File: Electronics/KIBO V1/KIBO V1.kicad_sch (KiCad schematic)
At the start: 46 parts, among them M1 Motor_Servo, M10 Motor_Servo, M11 Motor_Servo, M12 Motor_Servo, M13 Motor_DC, M14 Motor_DC, M15 Motor_DC, M16 Motor_DC, M17 Fan, M18 uMotor_Servo, M19 uMotor_Servo, M2 Motor_Servo, M20 uMotor_Servo, M21 uMotor_Servo, M3 Motor_Servo, M4 Motor_Servo, M5 Motor_Servo, M6 Motor_Servo, M7 Motor_Servo, M8 Motor_Servo, M9 Motor_Servo, Q1 TIP120, SW1 SW_SPST, U1 HC-SR04, U3 ESP32-DEVKITC, U4 GY-521, U5 DM-OLED096-636, U6 OV7670

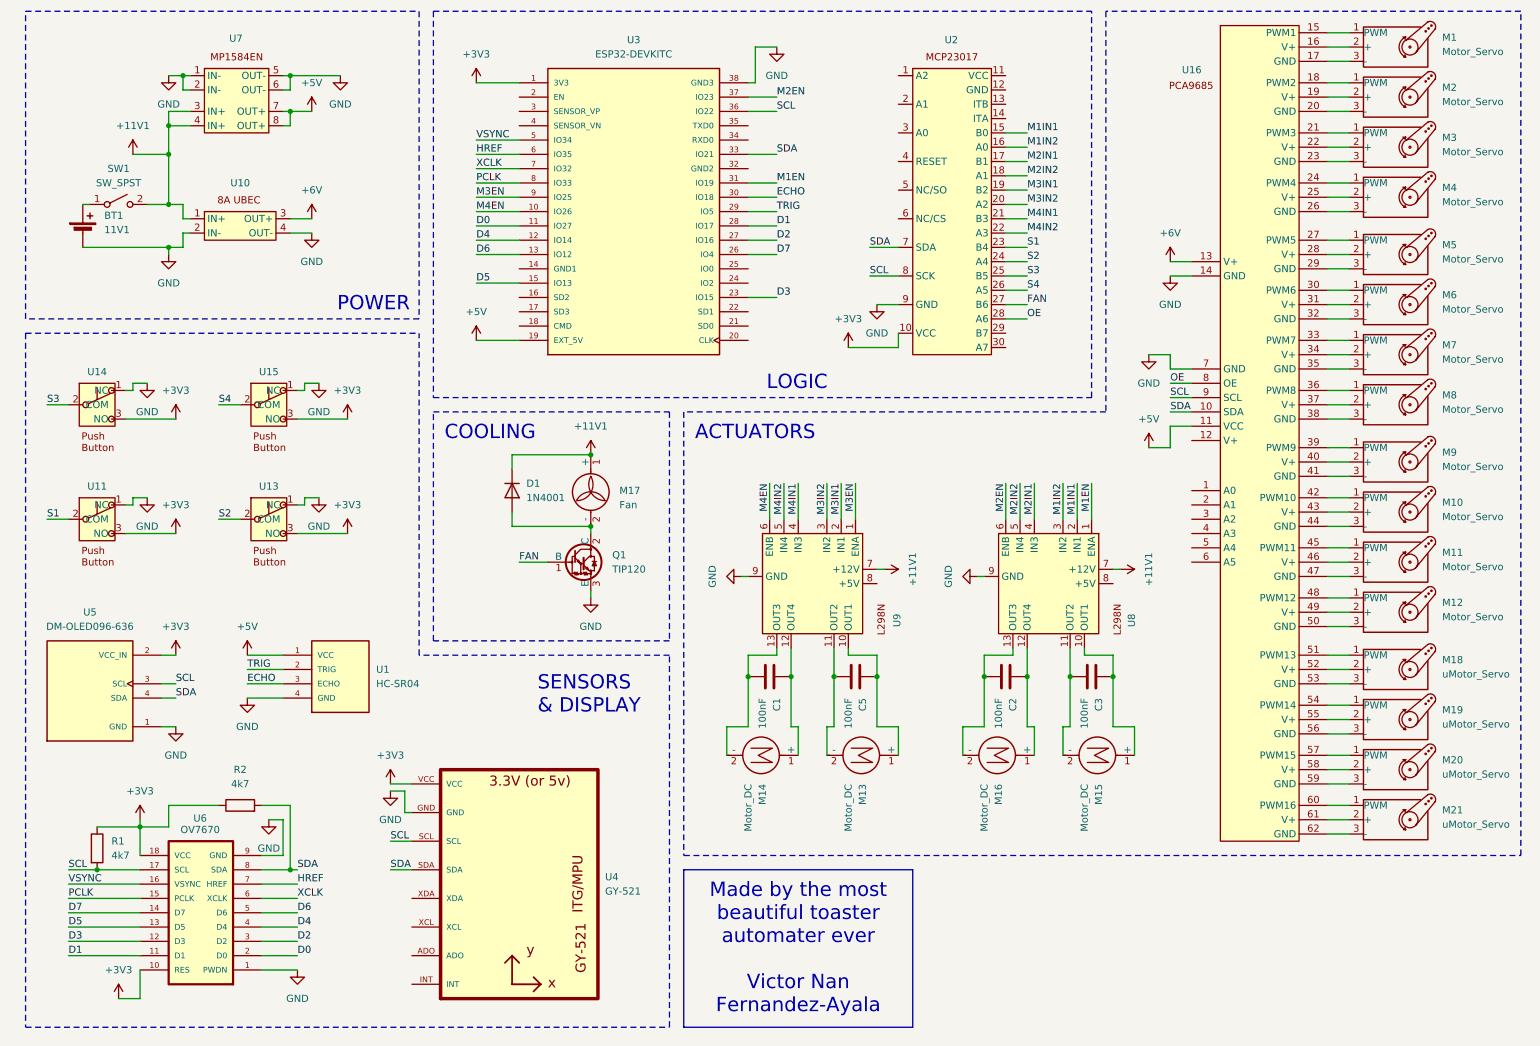
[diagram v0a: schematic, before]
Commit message: feat: added RGB LEDs and ESP32-CAM with PIR to schematic
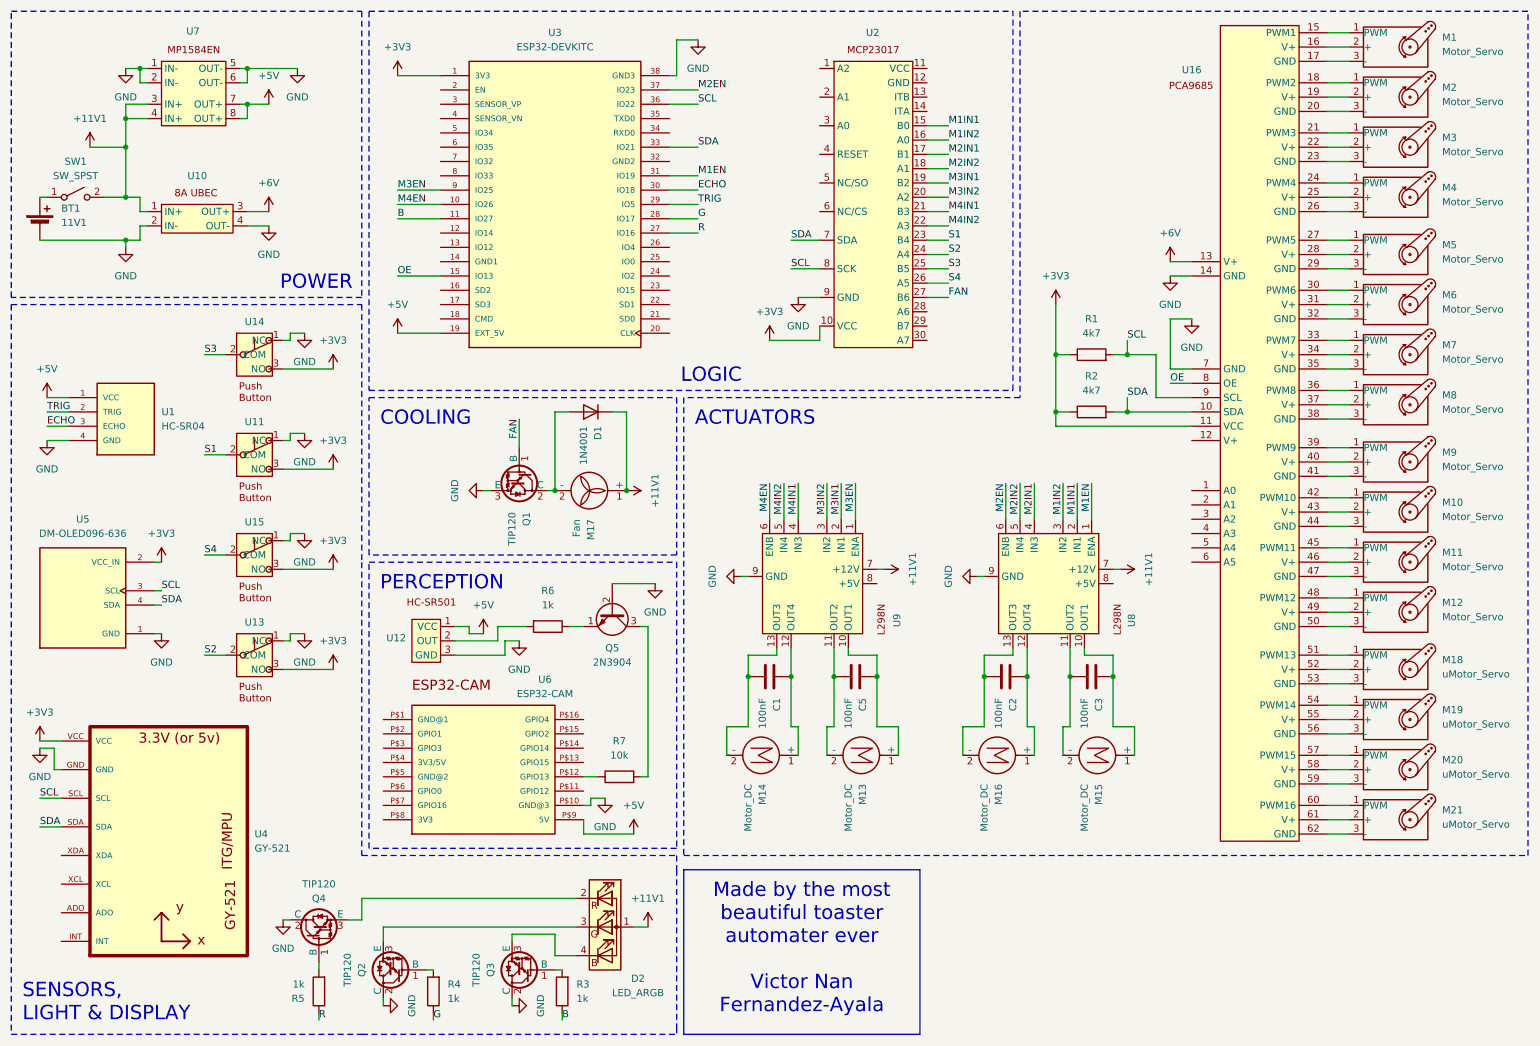
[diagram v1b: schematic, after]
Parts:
- removed U6: OV7670, OV7670:OV7670, symbol OV7670:OV7670_RST_PWDN
- added D2: LED_ARGB, symbol Device:LED_ARGB
- added Q2, Q3, Q4: TIP120, Package_TO_SOT_THT:TO-220-3_Vertical, symbol Transistor_BJT:TIP120
- added Q5: 2N3904, Package_TO_SOT_THT:TO-92_Inline, symbol Transistor_BJT:2N3904
- added R3, R4, R5, R6: 1k, symbol Device:R
- added R7: 10k, symbol Device:R
- added U12: ~, symbol PIRSensor_AZDelivery_HCSR501:HC-SR501
- added U6: ESP32-CAM, ESP32-CAM:ESP32-CAM, symbol ESP32-CAM:ESP32-CAM
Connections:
- net D5 is gone; now on net OE: U3.15 (IO13)
- net +11V1: now also D2.1 (A)
- net +3V3: now also U16.11 (VCC)
- net +5V: now also U12.1 (VCC), U6.P$9 (5V); no longer U16.11 (VCC)
- net GND: now also Q2.2 (C), Q3.2 (C), Q4.2 (C), Q5.2 (B), U12.3 (GND), U6.P$10 (GND@3)
- net OE: no longer U2.28 (A6)
- net D0 renamed B
- net B: now also R3.1
- net D1 renamed G
- net G: now also R4.1
- net D2 renamed R
- net R: now also R5.1
- net D3: no longer names the net of U3.23 (IO15)
- net D4: no longer names the net of U3.12 (IO14)
- net D6: no longer names the net of U3.13 (IO12)
- net D7: no longer names the net of U3.26 (IO4)
- net HREF: no longer names the net of U3.6 (IO35)
- net PCLK: no longer names the net of U3.8 (IO33)
- net VSYNC: no longer names the net of U3.5 (IO34)
- net XCLK: no longer names the net of U3.7 (IO32)
- new net: Q3.1 (B), R3.2
- new net: D2.4 (BK), Q3.3 (E)
- new net: D2.2 (RK), Q4.3 (E)
- new net: D2.3 (GK), Q2.3 (E)
- new net: Q2.1 (B), R4.2
- new net: R6.2, U12.2 (OUT)
- new net: Q4.1 (B), R5.2
- new net: R7.1, U6.P$12 (GPIO13)
- new net: Q5.3 (C), R7.2
- new net: Q5.1 (E), R6.1
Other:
- moved on the sheet: BT1, D1, M17, Q1, SW1, U1, U10, U11, U13, U14, U15, U2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

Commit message: feat: corrected schematics, finished all footprints and checked ERC
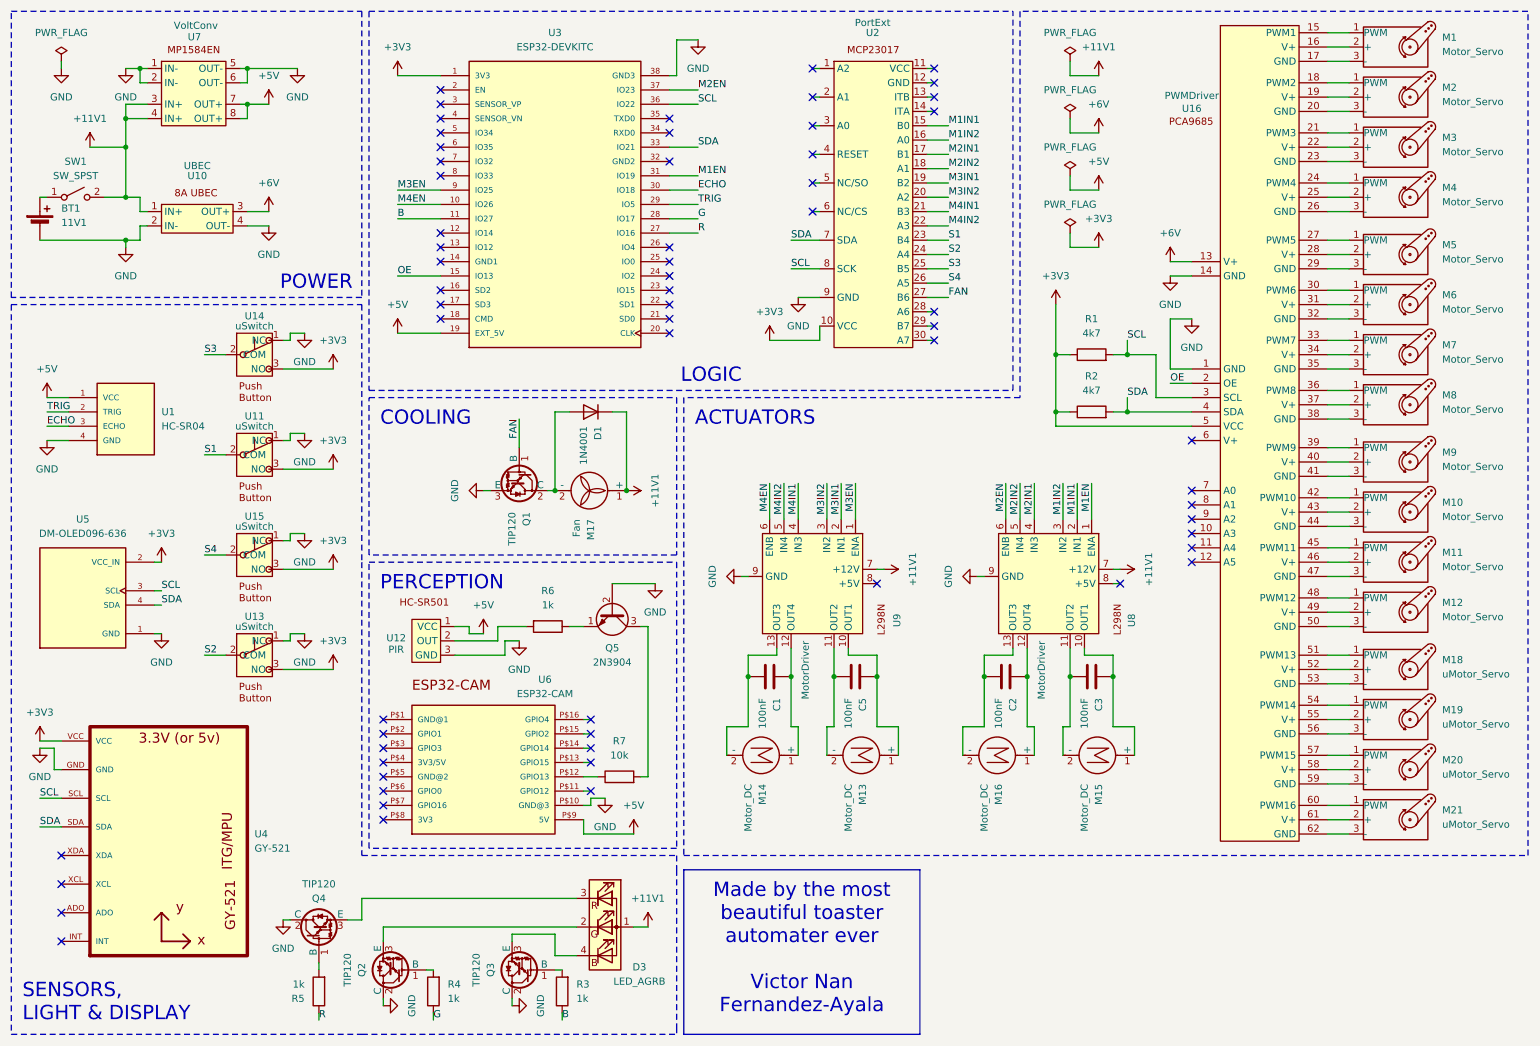
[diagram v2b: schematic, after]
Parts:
- removed D2: LED_ARGB, symbol Device:LED_ARGB
- added D3: LED_AGRB, Connector_PinHeader_2.54mm:PinHeader_1x04_P2.54mm_Vertical, symbol Device:LED_AGRB
- BT1: footprint (none) -> 2xBattery_Wire_Pads:2xBatterty_Wire_Pads
- C1, C2, C3, C5: footprint (none) -> Capacitor_THT:C_Disc_D5.0mm_W2.5mm_P5.00mm
- M17, SW1: footprint (none) -> Connector_Wire:SolderWire-0.75sqmm_1x02_P4.8mm_D1.25mm_OD2.3mm
- R1, R2, R3, R4, R5, R6, R7: footprint (none) -> Resistor_THT:R_Axial_DIN0207_L6.3mm_D2.5mm_P7.62mm_Horizontal
- U1: footprint HC-SR04:XCVR_HC-SR04 -> Connector_PinHeader_2.54mm:PinHeader_1x04_P2.54mm_Vertical
- U10: value ~ -> UBEC; footprint (none) -> 2xBattery_Wire_Pads:2xBatterty_Wire_Pads
- U11, U13, U14, U15: value ~ -> uSwitch; footprint (none) -> Connector_PinHeader_2.54mm:PinHeader_1x03_P2.54mm_Vertical
- U12: value ~ -> PIR
- U16: value ~ -> PWMDriver; footprint (none) -> Connector_PinHeader_2.54mm:PinHeader_1x05_P2.54mm_Vertical
- U2: value ~ -> PortExt; footprint (none) -> MCP23017:MCP23017
- U5: footprint DM-OLED096-636:MODULE_DM-OLED096-636 -> Connector_PinHeader_2.54mm:PinHeader_1x04_P2.54mm_Vertical
- U7: value ~ -> VoltConv; footprint (none) -> MP-1584EN:MP-1584EN
- U8, U9: value ~ -> MotorDriver; footprint (none) -> Connector_PinHeader_2.54mm:PinHeader_1x06_P2.54mm_Vertical
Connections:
- net +11V1: now also D3.1 (A)
- net +3V3: now also U16.5 (VCC); no longer U16.11 (VCC)
- net GND: now also U16.1 (GND); no longer U16.7 (GND)
- net OE: now also U16.2 (OE); no longer U16.8 (OE)
- net SCL: now also U16.3 (SCL); no longer U16.9 (SCL)
- net SDA: now also U16.4 (SDA); no longer U16.10 (SDA)
- net at Q3.3 (E): now also D3.4 (BK)
- net at Q4.3 (E): now also D3.3 (RK)
- net at Q2.3 (E): now also D3.2 (GK)
- no-connect marks 0 -> 62
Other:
- moved on the sheet: U12

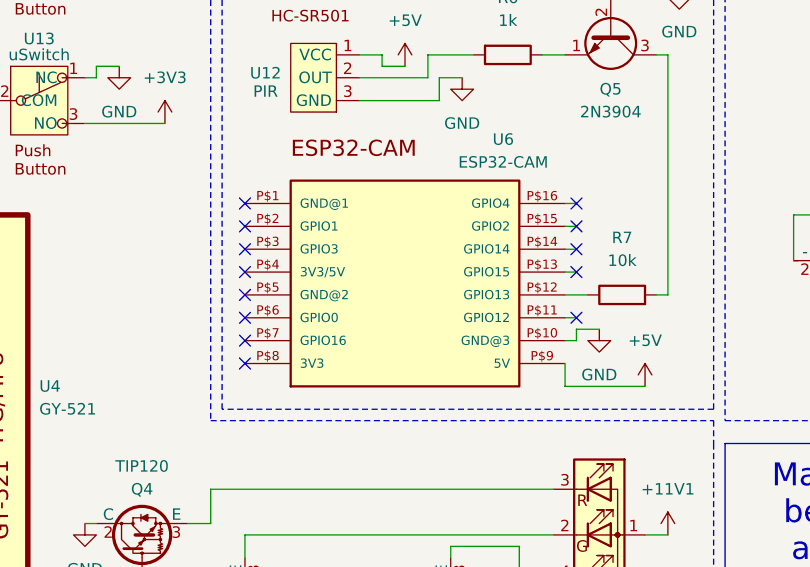
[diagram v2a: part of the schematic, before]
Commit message: feat: created PCB power pins for ESP32cam and added battery measurement script
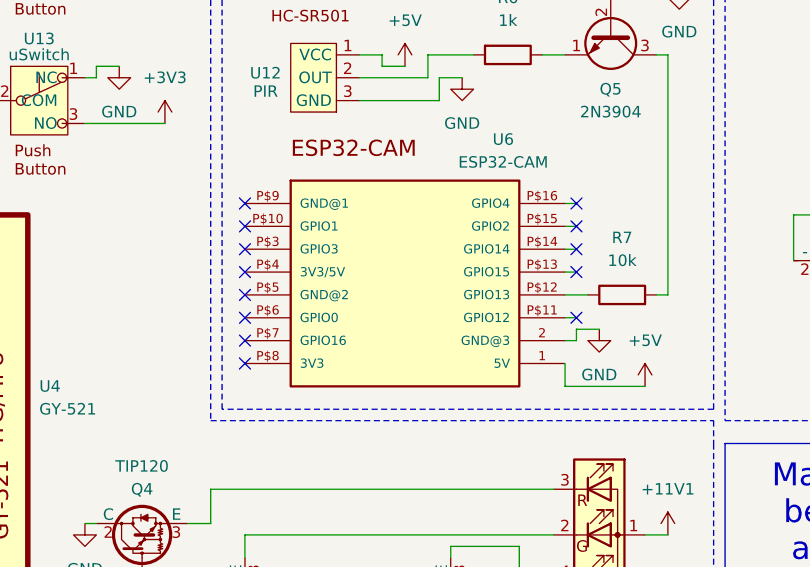
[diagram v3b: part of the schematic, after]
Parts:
- U6: footprint ESP32-CAM:ESP32-CAM -> Connector_PinHeader_2.54mm:PinHeader_1x02_P2.54mm_Vertical
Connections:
- net +5V: now also U6.1 (5V); no longer U6.P$9 (5V)
- net GND: now also U6.2 (GND@3); no longer U6.P$10 (GND@3)
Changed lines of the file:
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@@
 		(exclude_from_sim no)
 		(in_bom yes)
-		(on_board no)
+		(on_board yes)
 		(dnp no)
 		(property "Reference" "U6"
@@
 			)
 		)
-		(property "Footprint" "ESP32-CAM:ESP32-CAM"
+		(property "Footprint" "Connector_PinHeader_2.54mm:PinHeader_1x02_P2.54mm_Vertical"
 			(at 97.79 149.86 0)
 			(effects
@@
 			)
 		)
-		(pin "P$1"
+		(pin "2"
 		)
 		(pin "P$5"
@@
 		(pin "P$4"
 		)
-		(pin "P$2"
+		(pin "1"
 		)
 		(pin "P$15"
